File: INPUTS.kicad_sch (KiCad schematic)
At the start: 16 parts

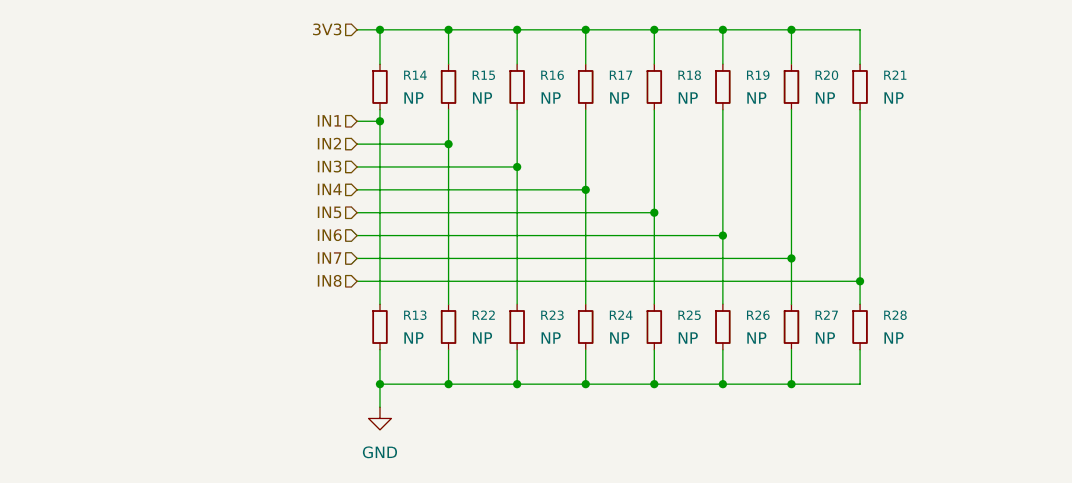
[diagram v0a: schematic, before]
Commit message: Add serial resistors on input pins
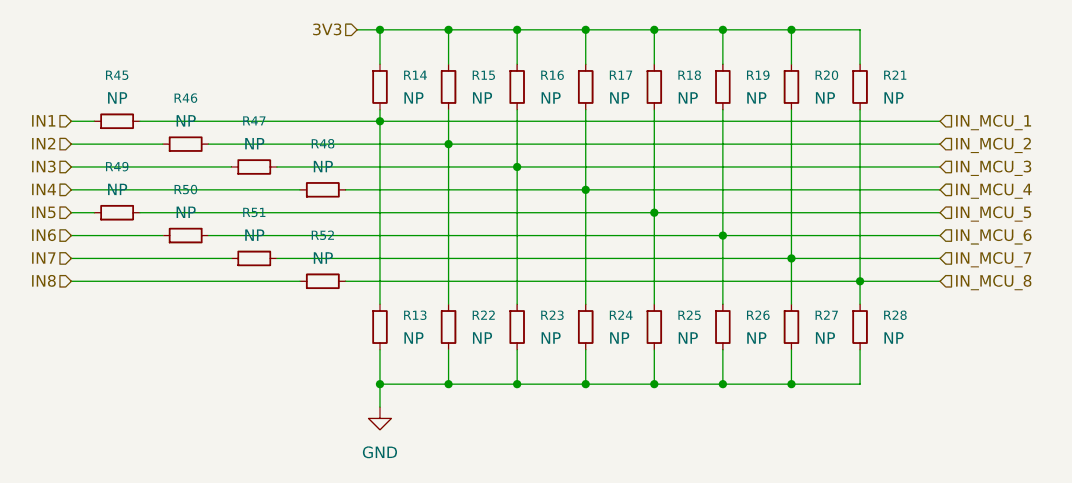
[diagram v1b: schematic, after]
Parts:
- added R45, R46, R47, R48, R49, R50, R51, R52: NP, Resistor_SMD:R_0603_1608Metric_Pad0.98x0.95mm_HandSolder, symbol Device:R_Small
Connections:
- net IN1: now also R45.1; no longer R13.1, R14.2
- net IN2: now also R46.1; no longer R15.2, R22.1
- net IN3: now also R47.1; no longer R16.2, R23.1
- net IN4: now also R48.1; no longer R17.2, R24.1
- net IN5: now also R49.1; no longer R18.2, R25.1
- net IN6: now also R50.1; no longer R19.2, R26.1
- net IN7: now also R51.1; no longer R20.2, R27.1
- net IN8: now also R52.1; no longer R21.2, R28.1
- new net IN_MCU_1: R13.1, R14.2, R45.2
- new net IN_MCU_2: R15.2, R22.1, R46.2
- new net IN_MCU_3: R16.2, R23.1, R47.2
- new net IN_MCU_4: R17.2, R24.1, R48.2
- new net IN_MCU_5: R18.2, R25.1, R49.2
- new net IN_MCU_6: R19.2, R26.1, R50.2
- new net IN_MCU_7: R20.2, R27.1, R51.2
- new net IN_MCU_8: R21.2, R28.1, R52.2
